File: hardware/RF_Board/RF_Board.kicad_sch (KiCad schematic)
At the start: 130 parts, among them J1 Conn_Coaxial, J2 Conn_01x04_Male, J3 Conn_Coaxial, J4 Conn_01x04_Male, J5 Conn_01x06_Female, J6 Conn_01x06_Female, J7 Conn_01x06_Female, J8 L77TSAH15SOL2RM8, Q1 2N7002, Q2 2N7002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

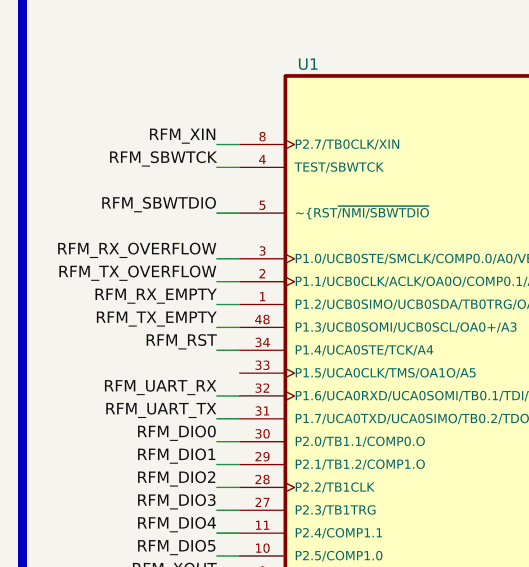
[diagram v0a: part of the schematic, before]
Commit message: RF board digital routing
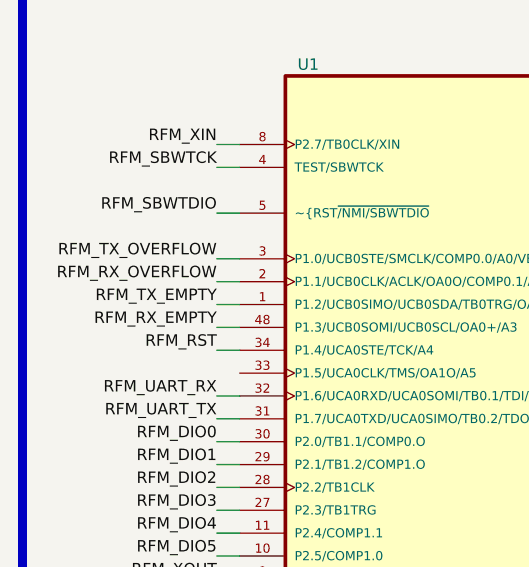
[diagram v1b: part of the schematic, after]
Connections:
- net RFM_RX_EMPTY: now also U1.48 (P1.3/UCB0SOMI/UCB0SCL/OA0+/A3); no longer U1.1 (P1.2/UCB0SIMO/UCB0SDA/TB0TRG/OA0-/A2/VEREF)
- net RFM_RX_OVERFLOW: now also U1.2 (P1.1/UCB0CLK/ACLK/OA0O/COMP0.1/A1); no longer U1.3 (P1.0/UCB0STE/SMCLK/COMP0.0/A0/VEREF+)
- net RFM_TX_EMPTY: now also U1.1 (P1.2/UCB0SIMO/UCB0SDA/TB0TRG/OA0-/A2/VEREF); no longer U1.48 (P1.3/UCB0SOMI/UCB0SCL/OA0+/A3)
- net RFM_TX_OVERFLOW: now also U1.3 (P1.0/UCB0STE/SMCLK/COMP0.0/A0/VEREF+); no longer U1.2 (P1.1/UCB0CLK/ACLK/OA0O/COMP0.1/A1)
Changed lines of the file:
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@@
+    (stroke (width 0) (type default) (color 0 0 0 0))
+  )
+  (wire (pts (xy 41.91 87.63) (xy 44.45 87.63))
     (stroke (width 0) (type default) (color 0 0 0 0))
   )
@@
     (stroke (width 0) (type default) (color 0 0 0 0))
   )
+  (wire (pts (xy 190.5 251.46) (xy 193.04 251.46))
+    (stroke (width 0) (type default) (color 0 0 0 0))
+  )
+  (wire (pts (xy 535.94 97.79) (xy 549.91 97.79))
+    (stroke (width 0) (type default) (color 0 0 0 0))
+  )
+  (wire (pts (xy 344.17 331.47) (xy 346.71 331.47))
+    (stroke (width 0) (type default) (color 0 0 0 0))
+  )
+  (wire (pts (xy 435.61 232.41) (xy 435.61 242.57))
+    (stroke (width 0) (type default) (color 0 0 0 0))
+  )
+  (wire (pts (xy 45.72 261.62) (xy 48.26 261.62))
+    (stroke (width 0) (type default) (color 0 0 0 0))
+  )
+  (wire (pts (xy 313.69 93.98) (xy 316.23 93.98))
+    (stroke (width 0) (type default) (color 0 0 0 0))
+  )
+  (wire (pts (xy 402.59 69.85) (xy 405.13 69.85))
+    (stroke (width 0) (type default) (color 0 0 0 0))
+  )
+  (wire (pts (xy 45.72 294.64) (xy 48.26 294.64))
+    (stroke (width 0) (type default) (color 0 0 0 0))
+  )
+  (wire (pts (xy 402.59 64.77) (xy 405.13 64.77))
+    (stroke (width 0) (type default) (color 0 0 0 0))
+  )
+  (wire (pts (xy 431.8 68.58) (xy 433.07 68.58))
+    (stroke (width 0) (type default) (color 0 0 0 0))
+  )
+  (wire (pts (xy 468.63 97.79) (xy 468.63 99.06))
+    (stroke (width 0) (type default) (color 0 0 0 0))
+  )
+  (wire (pts (xy 535.94 72.39) (xy 537.21 72.39))
+    (stroke (width 0) (type default) (color 0 0 0 0))
+  )
+  (wire (pts (xy 313.69 303.53) (xy 322.58 303.53))
+    (stroke (width 0) (type default) (color 0 0 0 0))
+  )
+  (wire (pts (xy 430.53 67.31) (xy 431.8 67.31))
+    (stroke (width 0) (type default) (color 0 0 0 0))
+  )
+  (wire (pts (xy 328.93 262.89) (xy 328.93 264.16))
+    (stroke (width 0) (type default) (color 0 0 0 0))
+  )
+  (wire (pts (xy 379.73 304.8) (xy 379.73 262.89))
+    (stroke (width 0) (type default) (color 0 0 0 0))
+  )
+  (wire (pts (xy 322.58 316.23) (xy 323.85 316.23))
+    (stroke (width 0) (type default) (color 0 0 0 0))
+  )
+  (wire (pts (xy 45.72 279.4) (xy 48.26 279.4))
+    (stroke (width 0) (type default) (color 0 0 0 0))
+  )
+  (wire (pts (xy 379.73 219.71) (xy 379.73 255.27))
+    (stroke (width 0) (type default) (color 0 0 0 0))
+  )
+  (wire (pts (xy 477.52 219.71) (xy 477.52 220.98))
+    (stroke (width 0) (type default) (color 0 0 0 0))
+  )
+  (wire (pts (xy 539.75 261.62) (xy 542.29 261.62))
+    (stroke (width 0) (type default) (color 0 0 0 0))
+  )
+  (wire (pts (xy 227.33 95.25) (xy 229.87 95.25))
+    (stroke (width 0) (type default) (color 0 0 0 0))
+  )
+  (wire (pts (xy 443.23 232.41) (xy 443.23 242.57))
+    (stroke (width 0) (type default) (color 0 0 0 0))
+  )
+  (wire (pts (xy 313.69 83.82) (xy 316.23 83.82))
+    (stroke (width 0) (type default) (color 0 0 0 0))
+  )
+  (wire (pts (xy 321.31 325.12) (xy 322.58 325.12))
+    (stroke (width 0) (type default) (color 0 0 0 0))
+  )
+  (wire (pts (xy 276.86 254) (xy 279.4 254))
+    (stroke (width 0) (type default) (color 0 0 0 0))
+  )
+  (wire (pts (xy 535.94 118.11) (xy 537.21 118.11))
+    (stroke (width 0) (type default) (color 0 0 0 0))
+  )
+  (wire (pts (xy 45.72 251.46) (xy 48.26 251.46))
+    (stroke (width 0) (type default) (color 0 0 0 0))
+  )
+  (wire (pts (xy 251.46 237.49) (xy 251.46 238.76))
+    (stroke (width 0) (type default) (color 0 0 0 0))
+  )
+  (wire (pts (xy 166.37 165.1) (xy 166.37 166.37))
+    (stroke (width 0) (type default) (color 0 0 0 0))
+  )
+  (wire (pts (xy 487.68 73.66) (xy 487.68 78.74))
+    (stroke (width 0) (type default) (color 0 0 0 0))
+  )
+  (wire (pts (xy 297.18 269.24) (xy 297.18 270.51))
+    (stroke (width 0) (type default) (color 0 0 0 0))
+  )
   (wire (pts (xy 41.91 92.71) (xy 44.45 92.71))
     (stroke (width 0) (type default) (color 0 0 0 0))
   )
-  (wire (pts (xy 190.5 251.46) (xy 193.04 251.46))
-    (stroke (width 0) (type default) (color 0 0 0 0))
-  )
-  (wire (pts (xy 535.94 97.79) (xy 549.91 97.79))
-    (stroke (width 0) (type default) (color 0 0 0 0))
-  )
-  (wire (pts (xy 344.17 331.47) (xy 346.71 331.47))
-    (stroke (width 0) (type default) (color 0 0 0 0))
-  )
-  (wire (pts (xy 435.61 232.41) (xy 435.61 242.57))
-    (stroke (width 0) (type default) (color 0 0 0 0))
-  )
-  (wire (pts (xy 45.72 261.62) (xy 48.26 261.62))
-    (stroke (width 0) (type default) (color 0 0 0 0))
-  )
-  (wire (pts (xy 313.69 93.98) (xy 316.23 93.98))
-    (stroke (width 0) (type default) (color 0 0 0 0))
-  )
-  (wire (pts (xy 402.59 69.85) (xy 405.13 69.85))
-    (stroke (width 0) (type default) (color 0 0 0 0))
-  )
-  (wire (pts (xy 45.72 294.64) (xy 48.26 294.64))
-    (stroke (width 0) (type default) (color 0 0 0 0))
-  )
-  (wire (pts (xy 402.59 64.77) (xy 405.13 64.77))
-    (stroke (width 0) (type default) (color 0 0 0 0))
-  )
-  (wire (pts (xy 431.8 68.58) (xy 433.07 68.58))
-    (stroke (width 0) (type default) (color 0 0 0 0))
-  )
-  (wire (pts (xy 468.63 97.79) (xy 468.63 99.06))
-    (stroke (width 0) (type default) (color 0 0 0 0))
-  )
-  (wire (pts (xy 535.94 72.39) (xy 537.21 72.39))
-    (stroke (width 0) (type default) (color 0 0 0 0))
-  )
-  (wire (pts (xy 313.69 303.53) (xy 322.58 303.53))
-    (stroke (width 0) (type default) (color 0 0 0 0))
-  )
-  (wire (pts (xy 430.53 67.31) (xy 431.8 67.31))
-    (stroke (width 0) (type default) (color 0 0 0 0))
-  )
-  (wire (pts (xy 328.93 262.89) (xy 328.93 264.16))
-    (stroke (width 0) (type default) (color 0 0 0 0))
-  )
-  (wire (pts (xy 379.73 304.8) (xy 379.73 262.89))
-    (stroke (width 0) (type default) (color 0 0 0 0))
-  )
-  (wire (pts (xy 322.58 316.23) (xy 323.85 316.23))
-    (stroke (width 0) (type default) (color 0 0 0 0))
-  )
-  (wire (pts (xy 45.72 279.4) (xy 48.26 279.4))
-    (stroke (width 0) (type default) (color 0 0 0 0))
-  )
-  (wire (pts (xy 379.73 219.71) (xy 379.73 255.27))
-    (stroke (width 0) (type default) (color 0 0 0 0))
-  )
-  (wire (pts (xy 477.52 219.71) (xy 477.52 220.98))
-    (stroke (width 0) (type default) (color 0 0 0 0))
-  )
-  (wire (pts (xy 539.75 261.62) (xy 542.29 261.62))
-    (stroke (width 0) (type default) (color 0 0 0 0))
-  )
-  (wire (pts (xy 227.33 95.25) (xy 229.87 95.25))
-    (stroke (width 0) (type default) (color 0 0 0 0))
-  )
-  (wire (pts (xy 443.23 232.41) (xy 443.23 242.57))
-    (stroke (width 0) (type default) (color 0 0 0 0))
-  )
-  (wire (pts (xy 313.69 83.82) (xy 316.23 83.82))
-    (stroke (width 0) (type default) (color 0 0 0 0))
-  )
-  (wire (pts (xy 321.31 325.12) (xy 322.58 325.12))
-    (stroke (width 0) (type default) (color 0 0 0 0))
-  )
-  (wire (pts (xy 276.86 254) (xy 279.4 254))
-    (stroke (width 0) (type default) (color 0 0 0 0))
-  )
-  (wire (pts (xy 535.94 118.11) (xy 537.21 118.11))
-    (stroke (width 0) (type default) (color 0 0 0 0))
-  )
-  (wire (pts (xy 45.72 251.46) (xy 48.26 251.46))
-    (stroke (width 0) (type default) (color 0 0 0 0))
-  )
-  (wire (pts (xy 251.46 237.49) (xy 251.46 238.76))
-    (stroke (width 0) (type default) (color 0 0 0 0))
-  )
-  (wire (pts (xy 166.37 165.1) (xy 166.37 166.37))
-    (stroke (width 0) (type default) (color 0 0 0 0))
-  )
-  (wire (pts (xy 487.68 73.66) (xy 487.68 78.74))
-    (stroke (width 0) (type default) (color 0 0 0 0))
-  )
-  (wire (pts (xy 297.18 269.24) (xy 297.18 270.51))
-    (stroke (width 0) (type default) (color 0 0 0 0))
-  )
   (wire (pts (xy 186.69 92.71) (xy 189.23 92.71))
     (stroke (width 0) (type default) (color 0 0 0 0))
@@
   )
   (wire (pts (xy 469.9 304.8) (xy 468.63 304.8))
+    (stroke (width 0) (type default) (color 0 0 0 0))
+  )
+  (wire (pts (xy 41.91 90.17) (xy 44.45 90.17))
     (stroke (width 0) (type default) (color 0 0 0 0))
   )
@@
     (stroke (width 0) (type default) (color 0 0 0 0))
   )
+  (wire (pts (xy 41.91 95.25) (xy 44.45 95.25))
+    (stroke (width 0) (type default) (color 0 0 0 0))
+  )
   (wire (pts (xy 481.33 99.06) (xy 481.33 97.79))
     (stroke (width 0) (type default) (color 0 0 0 0))
@@
     (stroke (width 0) (type default) (color 0 0 0 0))
   )
-  (wire (pts (xy 41.91 90.17) (xy 44.45 90.17))
-    (stroke (width 0) (type default) (color 0 0 0 0))
-  )
   (wire (pts (xy 468.63 97.79) (xy 481.33 97.79))
     (stroke (width 0) (type default) (color 0 0 0 0))
@@
     (stroke (width 0) (type default) (color 0 0 0 0))
   )
-  (wire (pts (xy 41.91 95.25) (xy 44.45 95.25))
-    (stroke (width 0) (type default) (color 0 0 0 0))
-  )
   (wire (pts (xy 435.61 242.57) (xy 435.61 251.46))
     (stroke (width 0) (type default) (color 0 0 0 0))
@@
   )
   (wire (pts (xy 323.85 325.12) (xy 322.58 325.12))
-    (stroke (width 0) (type default) (color 0 0 0 0))
-  )
-  (wire (pts (xy 41.91 87.63) (xy 44.45 87.63))
     (stroke (width 0) (type default) (color 0 0 0 0))
   )
@@
     (effects (font (size 1.27 1.27)) (justify right bottom))
   )
-  (label "RFM_RX_EMPTY" (at 41.91 92.71 180)
+  (label "RFM_RX_EMPTY" (at 41.91 95.25 180)
     (effects (font (size 1.27 1.27)) (justify right bottom))
   )
@@
     (effects (font (size 1.27 1.27)) (justify left bottom))
   )
-  (label "RFM_RX_OVERFLOW" (at 41.91 87.63 180)
+  (label "RFM_RX_OVERFLOW" (at 41.91 90.17 180)
     (effects (font (size 1.27 1.27)) (justify right bottom))
   )
@@
     (effects (font (size 1.27 1.27)) (justify left bottom))
   )
-  (label "RFM_TX_OVERFLOW" (at 41.91 90.17 180)
+  (label "RFM_TX_OVERFLOW" (at 41.91 87.63 180)
     (effects (font (size 1.27 1.27)) (justify right bottom))
   )
@@
     (effects (font (size 1.27 1.27)) (justify right bottom))
   )
-  (label "RFM_TX_EMPTY" (at 41.91 95.25 180)
-    (effects (font (size 1.27 1.27)) (justify right bottom))
-  )
+  (label "RFM_TX_EMPTY" (at 41.91 92.71 180)
+    (effects (font (size 1.27 1.27)) (justify right bottom))
+  )

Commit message: Finish RF board routing
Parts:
- removed R24, R25, R26, R27, R28, R29: 0, RF_Board_Footprints:R_0603_1608Metric, symbol RF_Board_Symbols:R_US
- added J9: Conn_01x09_Male, RF_Board_Footprints:PinHeader_1x09_P2.54mm_Vertical, symbol RF_Board_Symbols:Conn_01x09_Male
- D1, D7: footprint RF_Board_Footprints:D_SMB_Handsoldering -> RF_Board_Footprints:SOD882
- D2, D8: footprint RF_Board_Footprints:D_SMB_Handsoldering -> RF_Board_Footprints:D_SOD-523
- Q1, Q2: footprint RF_Board_Footprints:SOT-23-3 -> Package_TO_SOT_SMD:SOT-23
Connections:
- net CC2500_CSN: now also J9.4 (Pin_4)
- net CC2500_MISO: now also J9.7 (Pin_7)
- net CC2500_MOSI: now also J9.9 (Pin_9)
- net CC2500_RX_EMPTY: now also U2.48 (P1.3/UCB0SOMI/UCB0SCL/OA0+/A3); no longer U2.1 (P1.2/UCB0SIMO/UCB0SDA/TB0TRG/OA0-/A2/VEREF)
- net CC2500_RX_OVERFLOW: now also U2.2 (P1.1/UCB0CLK/ACLK/OA0O/COMP0.1/A1); no longer U2.3 (P1.0/UCB0STE/SMCLK/COMP0.0/A0/VEREF+)
- net CC2500_SCLK: now also J9.8 (Pin_8)
- net CC2500_TX_EMPTY: now also U2.1 (P1.2/UCB0SIMO/UCB0SDA/TB0TRG/OA0-/A2/VEREF); no longer U2.48 (P1.3/UCB0SOMI/UCB0SCL/OA0+/A3)
- net CC2500_TX_OVERFLOW: now also U2.3 (P1.0/UCB0STE/SMCLK/COMP0.0/A0/VEREF+); no longer U2.2 (P1.1/UCB0CLK/ACLK/OA0O/COMP0.1/A1)
- net GDO0: now also J9.5 (Pin_5)
- net GDO2: now also J9.6 (Pin_6)
- net GND: now also U10.9 (PAD), U11.9 (PAD)
- net RFM_AUX_CSN: now also J9.1 (Pin_1)
- net RFM_AUX_DIO0: now also J9.3 (Pin_3)
- net RFM_AUX_RST: now also J9.2 (Pin_2)

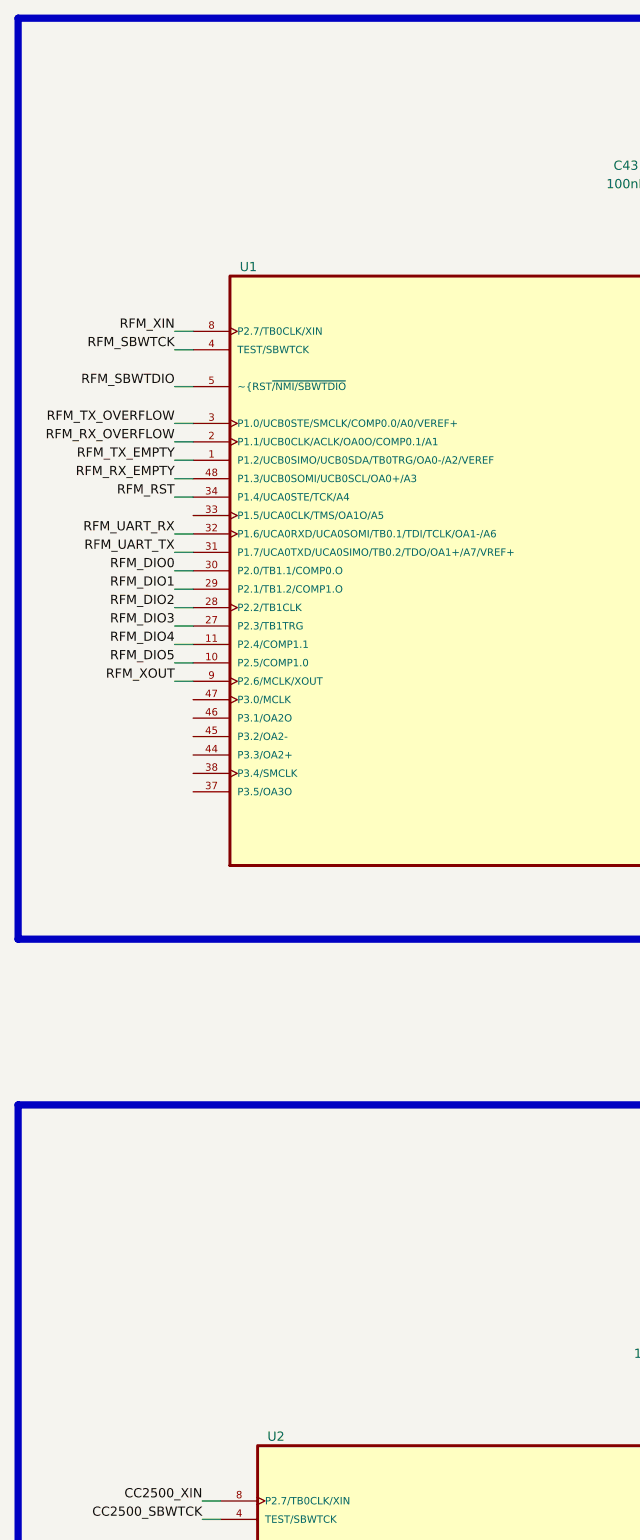
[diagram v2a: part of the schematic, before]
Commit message: finished RF board layout, sending to review
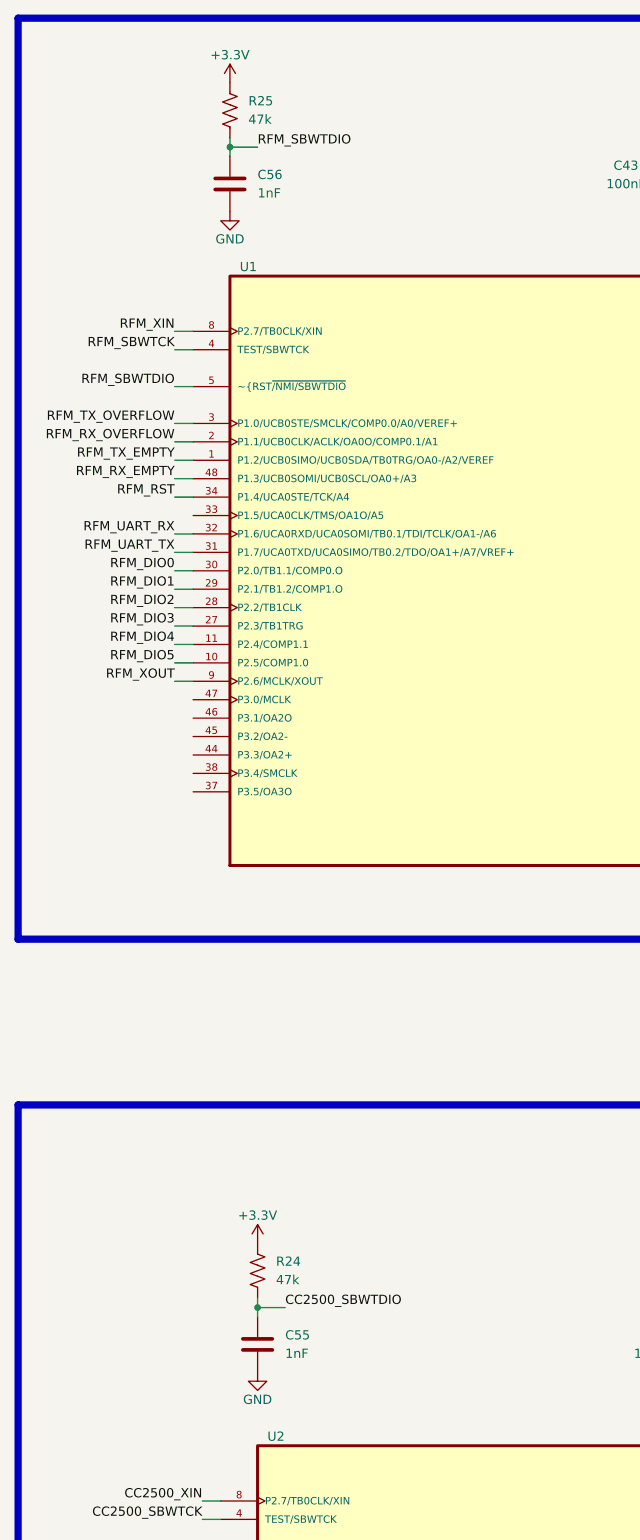
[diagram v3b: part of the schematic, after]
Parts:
- added C55, C56: 1nF, RF_Board_Footprints:C_0603_1608Metric, symbol RF_Board_Symbols:C
- added R24, R25: 47k, RF_Board_Footprints:R_0603_1608Metric, symbol RF_Board_Symbols:R_US
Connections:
- net +3.3V: now also R24.1, R25.1
- net CC2500_SBWTDIO: now also C55.1, R24.2
- net GND: now also C55.2, C56.2
- net RFM_SBWTDIO: now also C56.1, R25.2
